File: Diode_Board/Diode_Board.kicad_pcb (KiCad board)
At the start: 2 copper layers, 17.8 x 17.8 mm, 3 parts, among them J1 Conn_01x04

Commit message: Diode gerbers
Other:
- board size 17.8 x 17.8 mm -> 15.2 x 15.2 mm
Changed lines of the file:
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@@
     (pad_to_mask_clearance 0)
     (pcbplotparams
-      (layerselection 0x00010fc_ffffffff)
+      (layerselection 0x0001000_ffffffff)
       (disableapertmacros false)
       (usegerberextensions false)
@@
       (outputformat 1)
       (mirror false)
-      (drillshape 1)
+      (drillshape 0)
       (scaleselection 1)
-      (outputdirectory "")
+      (outputdirectory "./")
     )
   )
@@
     )
   )
-  (gr_rect (start 113.03 86.36) (end 130.81 104.14) (layer "Edge.Cuts") (width 0.2) (fill none))
+  (gr_rect (start 115.57 88.9) (end 130.81 104.14) (layer "Edge.Cuts") (width 0.2) (fill none))
   (segment (start 119.38 91.44) (end 127 91.44) (width 0.25) (layer "F.Cu") (net 1))
   (segment (start 117.79 100.01) (end 116.84 99.06) (width 0.25) (layer "F.Cu") (net 1))

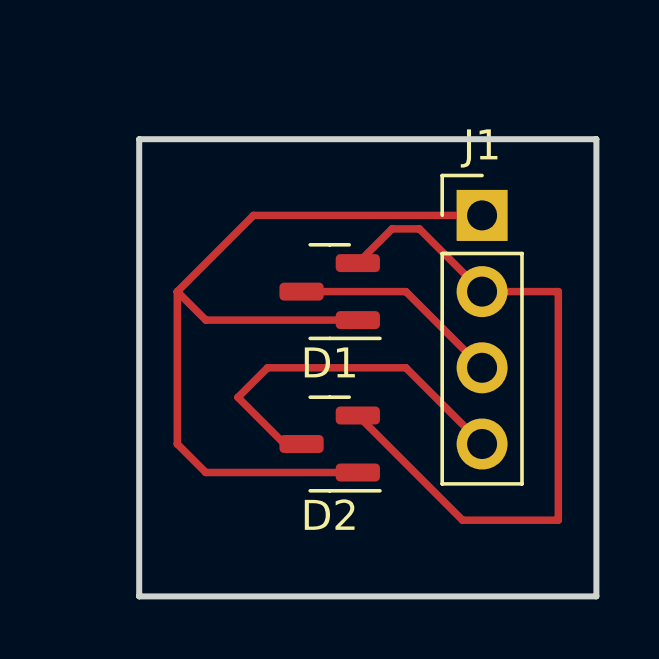
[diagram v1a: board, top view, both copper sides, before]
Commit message: Removed sensor from board
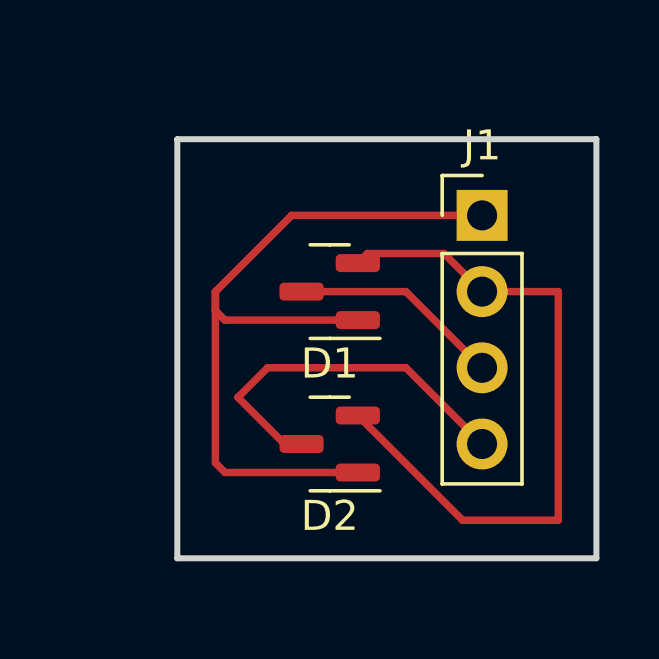
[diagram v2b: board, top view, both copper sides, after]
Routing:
- net Net-(D1-Pad1): track 29.1 -> 26.0 mm
- net Net-(D1-Pad2): track 23.8 -> 23.1 mm
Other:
- board size 15.2 x 15.2 mm -> 14 x 14 mm
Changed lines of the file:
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@@
     )
   )
-  (gr_rect (start 115.57 88.9) (end 130.81 104.14) (layer "Edge.Cuts") (width 0.2) (fill none))
-  (segment (start 119.38 91.44) (end 127 91.44) (width 0.25) (layer "F.Cu") (net 1))
-  (segment (start 117.79 100.01) (end 116.84 99.06) (width 0.25) (layer "F.Cu") (net 1))
-  (segment (start 122.8575 100.01) (end 117.79 100.01) (width 0.25) (layer "F.Cu") (net 1))
-  (segment (start 116.84 93.98) (end 119.38 91.44) (width 0.25) (layer "F.Cu") (net 1))
-  (segment (start 117.79 94.93) (end 116.84 93.98) (width 0.25) (layer "F.Cu") (net 1))
-  (segment (start 122.8575 94.93) (end 117.79 94.93) (width 0.25) (layer "F.Cu") (net 1))
-  (segment (start 116.84 99.06) (end 116.84 93.98) (width 0.25) (layer "F.Cu") (net 1))
+  (gr_rect (start 116.84 88.9) (end 130.81 102.87) (layer "Edge.Cuts") (width 0.2) (fill none))
+  (segment (start 118.425 94.93) (end 118.11 94.615) (width 0.25) (layer "F.Cu") (net 1))
+  (segment (start 122.8575 100.01) (end 118.43 100.01) (width 0.25) (layer "F.Cu") (net 1))
+  (segment (start 118.43 100.01) (end 118.11 99.69) (width 0.25) (layer "F.Cu") (net 1))
+  (segment (start 120.65 91.44) (end 127 91.44) (width 0.25) (layer "F.Cu") (net 1))
+  (segment (start 118.11 93.98) (end 120.65 91.44) (width 0.25) (layer "F.Cu") (net 1))
+  (segment (start 118.11 99.69) (end 118.11 93.98) (width 0.25) (layer "F.Cu") (net 1))
+  (segment (start 118.11 94.615) (end 118.11 93.98) (width 0.25) (layer "F.Cu") (net 1))
+  (segment (start 122.8575 94.93) (end 118.425 94.93) (width 0.25) (layer "F.Cu") (net 1))
   (segment (start 129.54 101.6) (end 129.54 93.98) (width 0.25) (layer "F.Cu") (net 2))
   (segment (start 126.3475 101.6) (end 129.54 101.6) (width 0.25) (layer "F.Cu") (net 2))
   (segment (start 122.8575 98.11) (end 126.3475 101.6) (width 0.25) (layer "F.Cu") (net 2))
-  (segment (start 124.91 91.89) (end 127 93.98) (width 0.25) (layer "F.Cu") (net 2))
-  (segment (start 123.9975 91.89) (end 124.91 91.89) (width 0.25) (layer "F.Cu") (net 2))
+  (segment (start 125.73 92.71) (end 127 93.98) (width 0.25) (layer "F.Cu") (net 2))
+  (segment (start 123.1775 92.71) (end 125.73 92.71) (width 0.25) (layer "F.Cu") (net 2))
   (segment (start 129.54 93.98) (end 127 93.98) (width 0.25) (layer "F.Cu") (net 2))
-  (segment (start 122.8575 93.03) (end 123.9975 91.89) (width 0.25) (layer "F.Cu") (net 2))
+  (segment (start 122.8575 93.03) (end 123.1775 92.71) (width 0.25) (layer "F.Cu") (net 2))
   (segment (start 124.46 93.98) (end 127 96.52) (width 0.25) (layer "F.Cu") (net 3))
   (segment (start 120.9825 93.98) (end 124.46 93.98) (width 0.25) (layer "F.Cu") (net 3))
